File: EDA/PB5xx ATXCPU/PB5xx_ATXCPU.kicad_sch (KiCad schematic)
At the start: 8 parts, among them J1 GND Sense, J2 PWR Battery, J3 GND Main, J4 PWR Main, J5 ATX CPU

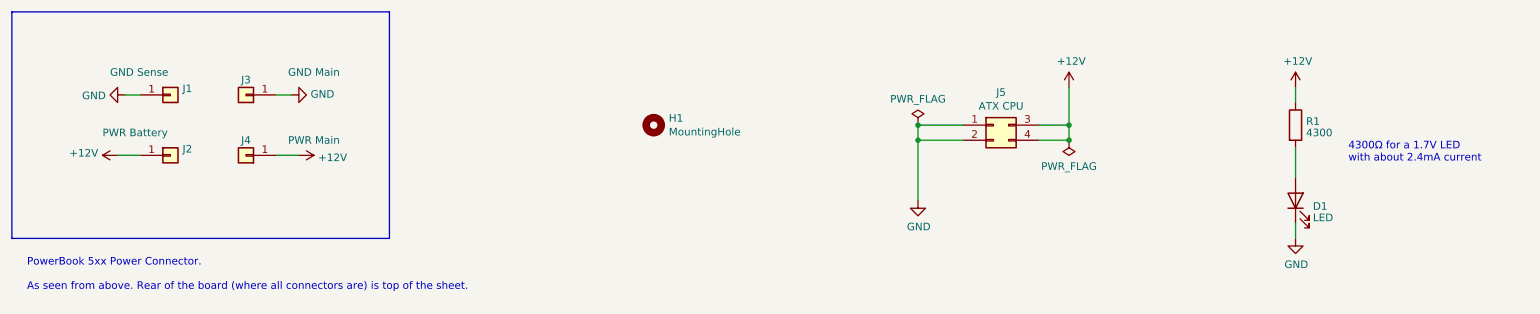
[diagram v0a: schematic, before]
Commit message: PB5xx ATXCPU v1.3: back to THT, moded to use IDC sockets
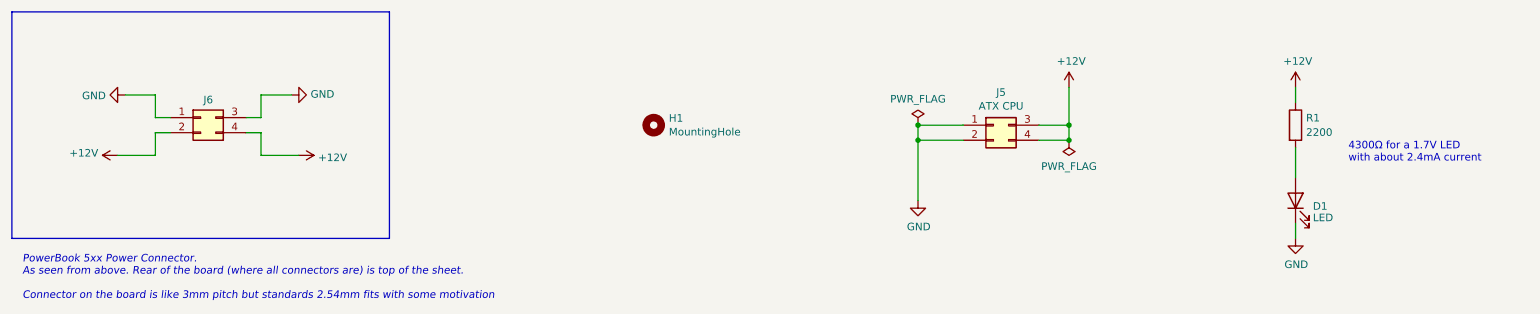
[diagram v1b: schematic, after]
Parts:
- removed J1: GND Sense, Connector_PinHeader_2.54mm:PinHeader_1x01_P2.54mm_Vertical, symbol Connector_Generic:Conn_01x01
- removed J2: PWR Battery, Connector_PinHeader_2.54mm:PinHeader_1x01_P2.54mm_Vertical, symbol Connector_Generic:Conn_01x01
- removed J3: GND Main, Connector_PinHeader_2.54mm:PinHeader_1x01_P2.54mm_Vertical, symbol Connector_Generic:Conn_01x01
- removed J4: PWR Main, Connector_PinHeader_2.54mm:PinHeader_1x01_P2.54mm_Vertical, symbol Connector_Generic:Conn_01x01
- added J6: Conn_02x02_Top_Bottom, Connector_PinSocket_2.54mm:PinSocket_2x02_P2.54mm_Vertical, symbol Connector_Generic:Conn_02x02_Top_Bottom
- D1: footprint LED_SMD:LED_0805_2012Metric -> LED_THT:LED_D5.0mm
- R1: value 4300 -> 2200; footprint Resistor_SMD:R_0805_2012Metric -> Resistor_THT:R_Axial_DIN0207_L6.3mm_D2.5mm_P7.62mm_Horizontal
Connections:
- net +12V: now also J6.2 (Pin_2), J6.4 (Pin_4)
- net GND: now also J6.1 (Pin_1), J6.3 (Pin_3)
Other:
- note added: "PowerBook 5xx Power Connector. As seen from above. Rear of the board (where all connectors are) is top of the sheet. Connector on the board is like 3mm pitch but standards 2.54mm fits with some motivation"
- note removed: "PowerBook 5xx Power Connector. As seen from above. Rear of the board (where all connectors are) is top of the sheet."

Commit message: PB5xx ATXCPU v1.4: add provisioning for small decoupling capacitor
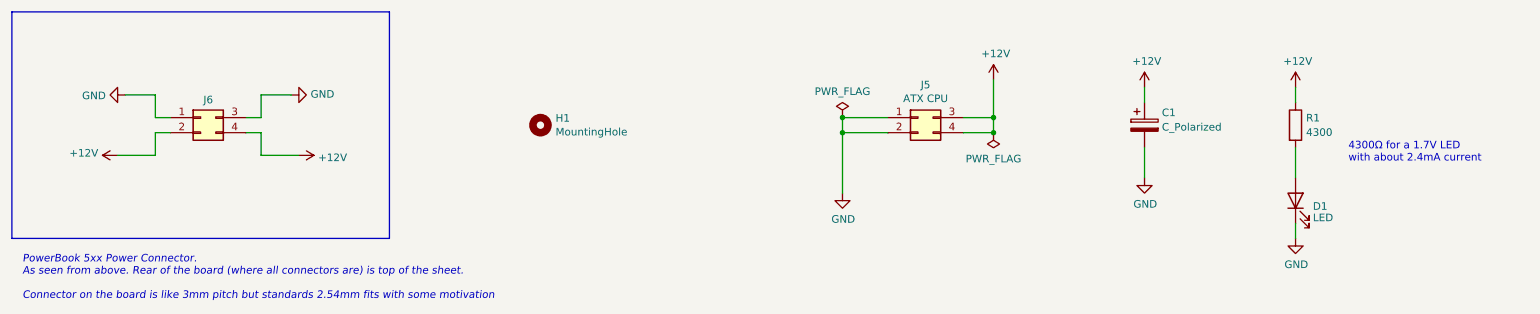
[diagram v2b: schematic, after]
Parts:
- added C1: C_Polarized, Capacitor_THT:CP_Radial_D8.0mm_P3.50mm, symbol Device:C_Polarized
- R1: value 2200 -> 4300
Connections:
- net +12V: now also C1.1
- net GND: now also C1.2
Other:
- moved on the sheet: H1, J5
